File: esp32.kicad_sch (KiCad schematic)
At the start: 15 parts, among them J2 Conn_01x05_Pin, Q3 MMBT3904, Q4 MMBT3904, U14 S32K324NHT1MPBST, Y1 ECS-2520MV-xxx-xx

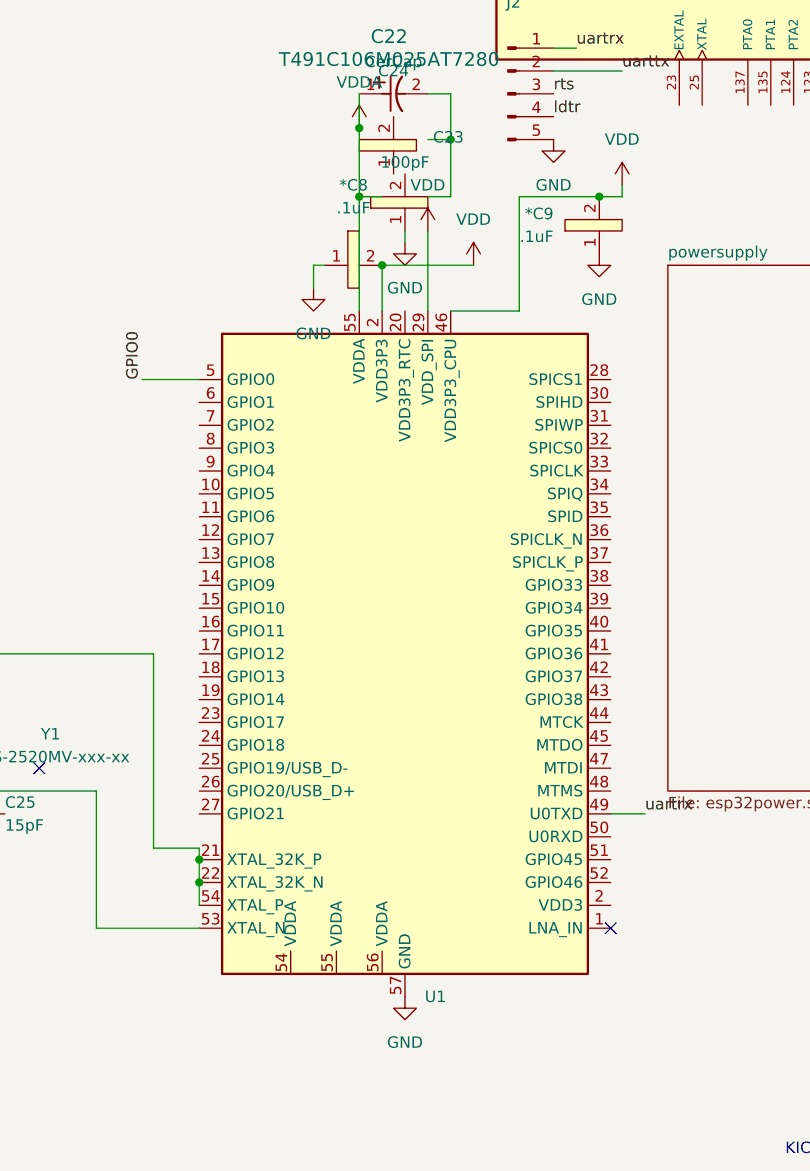
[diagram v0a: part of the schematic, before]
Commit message: added revised esp32 rto common library
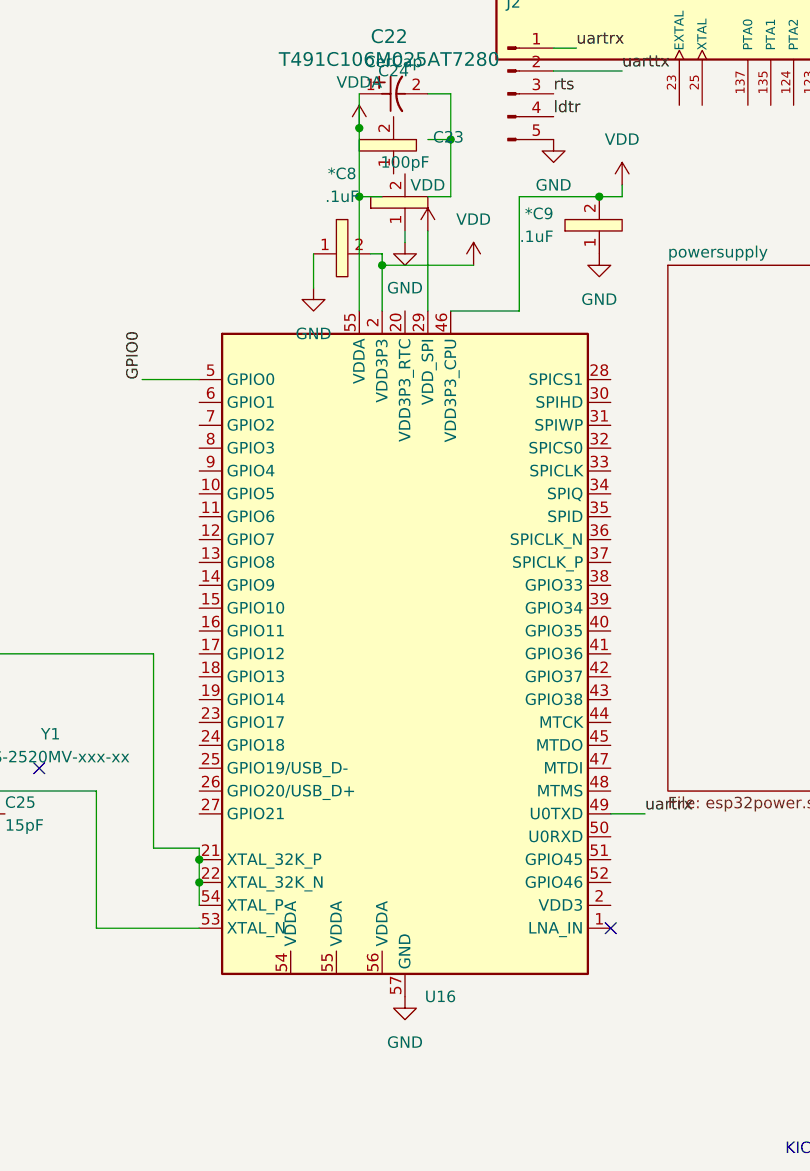
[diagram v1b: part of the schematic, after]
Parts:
- removed U1: ~, RF_Module:ESP32-S3-WROOM-1, symbol esp32lib:myEsp32
- added U16: ~, symbol common:ESP32S3Bruce
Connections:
- net GND: now also U16.57 (GND)
- net GPIO0: now also U16.5 (GPIO0)
- net VDD: now also U16.2 (VDD3P3), U16.29 (VDD_SPI), U16.3 (VDD3P3), U16.46 (VDD3P3_CPU)
- net VDDA: now also U16.55 (VDDA), U16.56 (VDDA)
- net uartrx: now also U16.49 (U0TXD)
- net at Y1.1 (Tri-State): now also U16.21 (XTAL_32K_P), U16.22 (XTAL_32K_N), U16.54 (XTAL_P)
- net at Y1.3 (OUT): now also U16.53 (XTAL_N)
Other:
- moved on the sheet: *C8
